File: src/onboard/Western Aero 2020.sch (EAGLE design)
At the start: 84 parts, among them J1 PITOT, J10 ANA_IO, J11 PWR, J2 BUZZER, J3 RX2/TX2, J4 RX3/TX3, J5 SPI, J6 DIG_IO, J7 RX1/TX1, J8 DIG_IO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

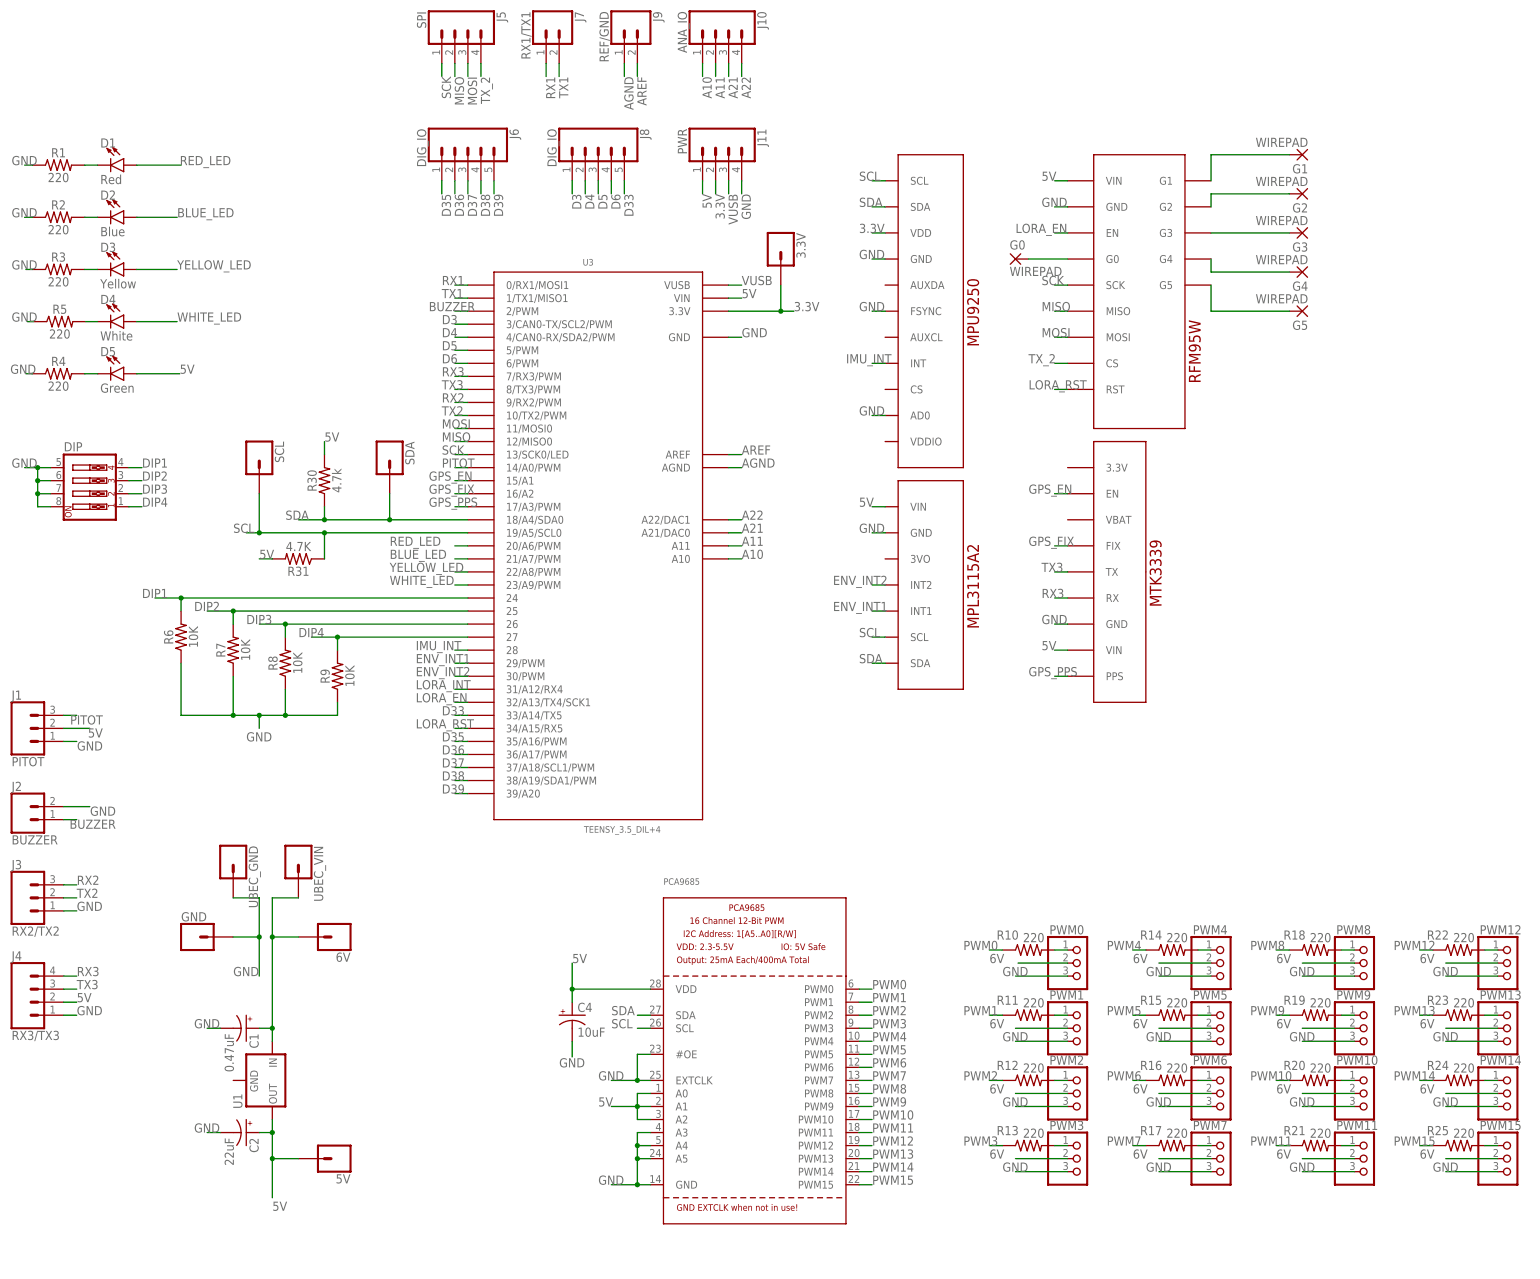
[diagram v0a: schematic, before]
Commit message: Fixed some connections and upgraded to ver 2.0
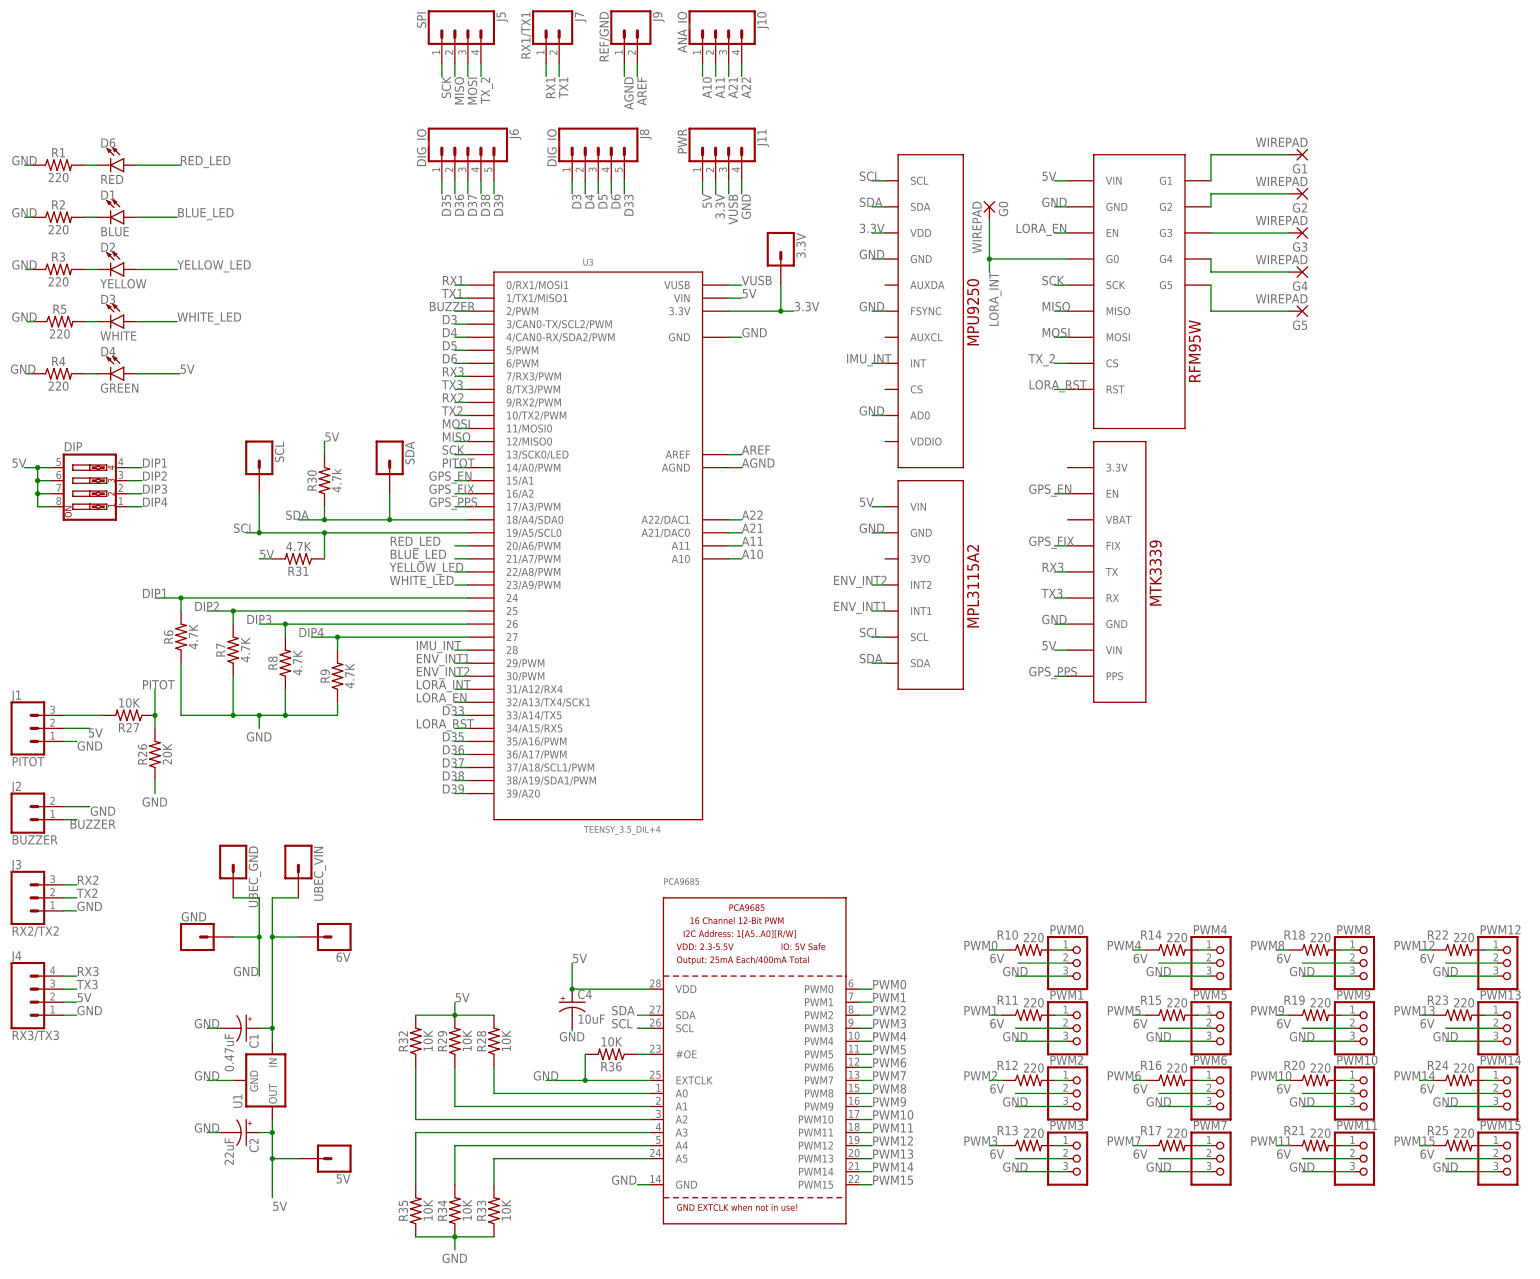
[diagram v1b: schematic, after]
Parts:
- removed D5: Green, SparkFun-LED:LED3MM
- added D6: RED, SparkFun-LED:LED5MM
- added R26: 20K, SparkFun-Resistors:330OHM-HORIZ-1/10W-5%
- added R27, R28, R29, R32, R33, R34, R35, R36: 10K, SparkFun-Resistors:330OHM-HORIZ-1/10W-5%
- D1: value Red -> BLUE; device SparkFun-LED:LED3MM -> SparkFun-LED:LED5MM
- D2: value Blue -> YELLOW; device SparkFun-LED:LED3MM -> SparkFun-LED:LED5MM
- D3: value Yellow -> WHITE; device SparkFun-LED:LED3MM -> SparkFun-LED:LED5MM
- D4: value White -> GREEN; device SparkFun-LED:LED3MM -> SparkFun-LED:LED5MM
- R6, R7, R8, R9: value 10K -> 4.7K
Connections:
- new net N$28: J1.3, R27.2
- new net N$29: PCA9685.A5, R33.2
- new net N$30: PCA9685.#OE, R36.1
- new net N$31: PCA9685.A4, R34.2
- new net N$32: PCA9685.A3, R35.2
- new net N$33: PCA9685.A2, R32.1
- new net N$34: PCA9685.A1, R29.1
- net 5V: now also D4.A, DIP.5, DIP.6, DIP.7, DIP.8, R28.2, R29.2, R32.2; no longer D5.A, PCA9685.A0, PCA9685.A1, PCA9685.A2
- net BLUE_LED: now also D1.A; no longer D2.A
- net GND: now also R26.1, R33.1, R34.1, R35.1, R36.2, U1.GND; no longer DIP.5, DIP.6, DIP.7, DIP.8, PCA9685.#OE, PCA9685.A3, PCA9685.A4, PCA9685.A5
- net LORA_INT: now also G0.P, U8.G0
- net N$2: now also D6.C; no longer D1.C
- net N$27: now also PCA9685.A0, R28.1; no longer G0.P, U8.G0
- net N$3: now also D1.C; no longer D2.C
- net N$4: now also D2.C; no longer D3.C
- net N$5: now also D3.C; no longer D4.C
- net N$6: now also D4.C; no longer D5.C
- net PITOT: now also R26.2, R27.1; no longer J1.3
- net RED_LED: now also D6.A; no longer D1.A
- net RX3: now also U9.TX; no longer U9.RX
- net TX3: now also U9.RX; no longer U9.TX
- net WHITE_LED: now also D3.A; no longer D4.A
- net YELLOW_LED: now also D2.A; no longer D3.A
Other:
- moved on the sheet: C4, D1, D2, D3, D4, G0

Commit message: Release v2.0
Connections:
- removed net TX_2: J5.4, U8.CS
- net TX2: now also J5.4, U8.CS
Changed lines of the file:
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@@
 <label x="-5.08" y="144.78" size="1.778" layer="95"/>
+</segment>
+<segment>
+<pinref part="U8" gate="G$1" pin="CS"/>
+<wire x1="116.84" y1="154.94" x2="114.3" y2="154.94" width="0.1524" layer="91"/>
+<label x="109.22" y="154.94" size="1.778" layer="95"/>
+</segment>
+<segment>
+<pinref part="J5" gate="G$1" pin="4"/>
+<wire x1="2.54" y1="213.36" x2="2.54" y2="210.82" width="0.1524" layer="91"/>
+<label x="2.54" y="210.82" size="1.778" layer="95" rot="R270"/>
 </segment>
 </net>
@@
 </segment>
 </net>
-<net name="TX_2" class="0">
-<segment>
-<pinref part="U8" gate="G$1" pin="CS"/>
-<wire x1="116.84" y1="154.94" x2="114.3" y2="154.94" width="0.1524" layer="91"/>
-<label x="109.22" y="154.94" size="1.778" layer="95"/>
-</segment>
-<segment>
-<pinref part="J5" gate="G$1" pin="4"/>
-<wire x1="2.54" y1="213.36" x2="2.54" y2="210.82" width="0.1524" layer="91"/>
-<label x="2.54" y="210.82" size="1.778" layer="95" rot="R270"/>
-</segment>
-</net>
